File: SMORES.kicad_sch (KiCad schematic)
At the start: 41 parts, among them J1 USB_C_Receptacle_USB2.0_14P, SW1 Power, SW2 Reset, SW3 SW0, U2 BQ24075RGT, U3 ICM45686, U4 XC6220B331MR, U5 1532H, U6 QMC6309, U7 E73-2G4M08S1C, Y2 32.768kHz

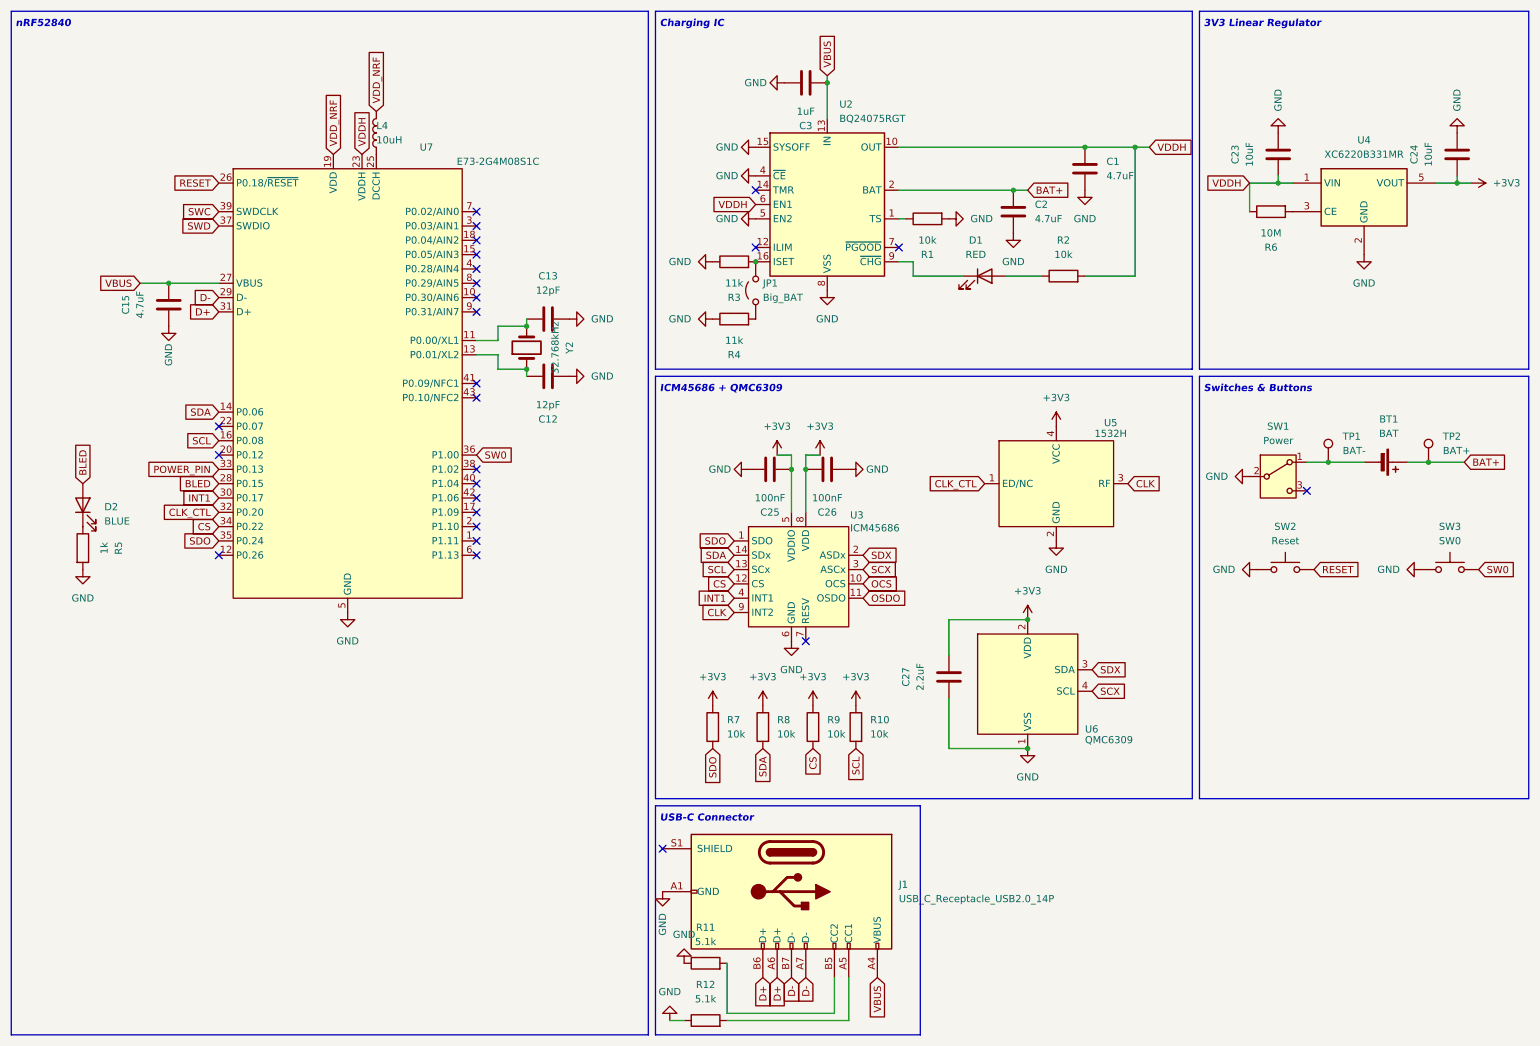
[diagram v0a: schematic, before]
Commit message: Remove LDO and peripherals
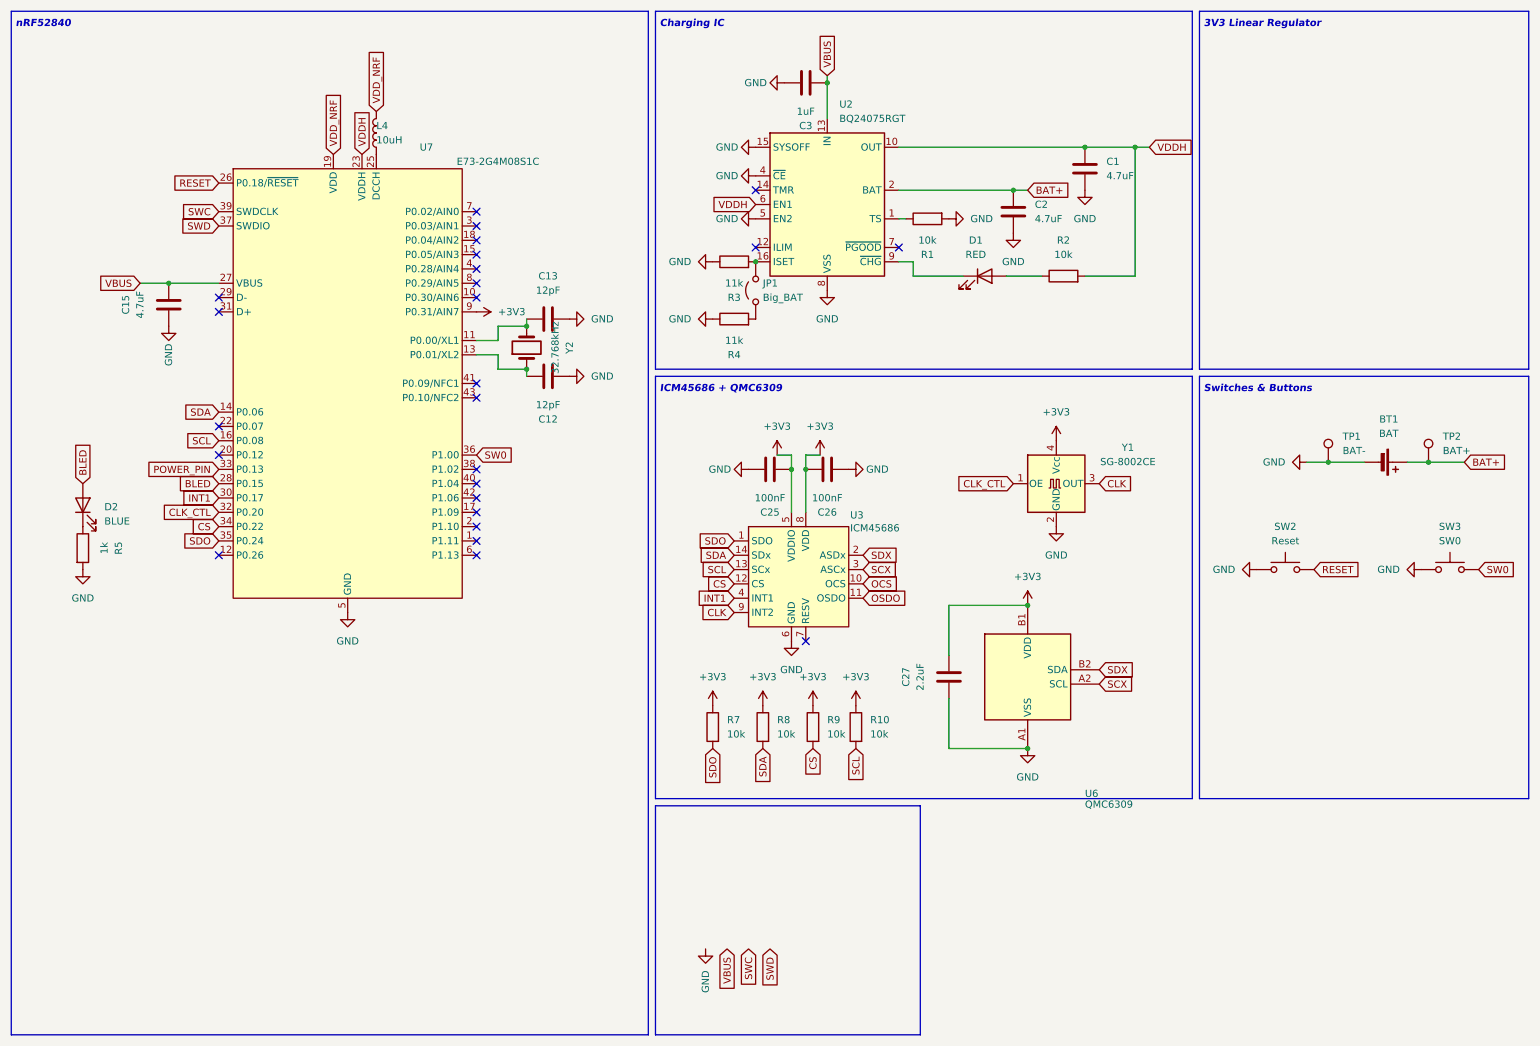
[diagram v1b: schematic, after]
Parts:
- removed C23, C24: 10uF, Capacitor_SMD:C_0603_1608Metric, symbol Device:C
- removed J1: USB_C_Receptacle_USB2.0_14P, Connector_USB:USB_C_Receptacle_HRO_TYPE-C-31-M-12, symbol Connector:USB_C_Receptacle_USB2.0_14P
- removed R11, R12: 5.1k, Capacitor_SMD:C_0603_1608Metric, symbol Device:R
- removed R6: 10M, Resistor_SMD:R_0402_1005Metric, symbol Device:R
- removed SW1: Power, SMORES:SW_SPDT_Shouhan_MSK12C02, symbol Switch:SW_SPDT
- removed U4: XC6220B331MR, Package_TO_SOT_SMD:SOT-23-5, symbol Regulator_Linear:XC6220B331MR
- removed U5: 1532H, Crystal:Crystal_SMD_3225-4Pin_3.2x2.5mm, symbol SlimeVR_Smol:1532H
- added Y1: SG-8002CE, Oscillator:Oscillator_SMD_SeikoEpson_SG8002CE-4Pin_3.2x2.5mm, symbol Oscillator:SG-8002CE
- U3: footprint ICM_SLIME:IC_ICM-45686 -> ICM-45686:IC_ICM-45686
- U6: footprint Custom:WLCSP-4_0.8x0.8mm_Layout2x2_P0.4mm -> QMC6309:IC_QMC6309; symbol SlimeVR_Smol:QMC6309 -> QMC6309:QMC6309
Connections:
- net +3V3: now also U6.B1 (VDD), U7.9 (P0.31/AIN7), Y1.4 (Vcc); no longer U6.2 (VDD)
- net CLK: now also Y1.3 (OUT)
- net CLK_CTL: now also Y1.1 (OE)
- net GND: now also BT1.2 (-), TP1.1, U6.A1 (VSS), Y1.2 (GND); no longer U6.1 (VSS)
- net SCX: now also U6.A2 (SCL); no longer U6.4 (SCL)
- net SDX: now also U6.B2 (SDA); no longer U6.3 (SDA)
- net D+: no longer names the net of U7.31 (D+)
- net D-: no longer names the net of U7.29 (D-)
- no-connect marks 26 -> 25
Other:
- note removed: "USB-C Connector"
- moved on the sheet: U6

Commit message: Redesign entire PCB and make it smaller
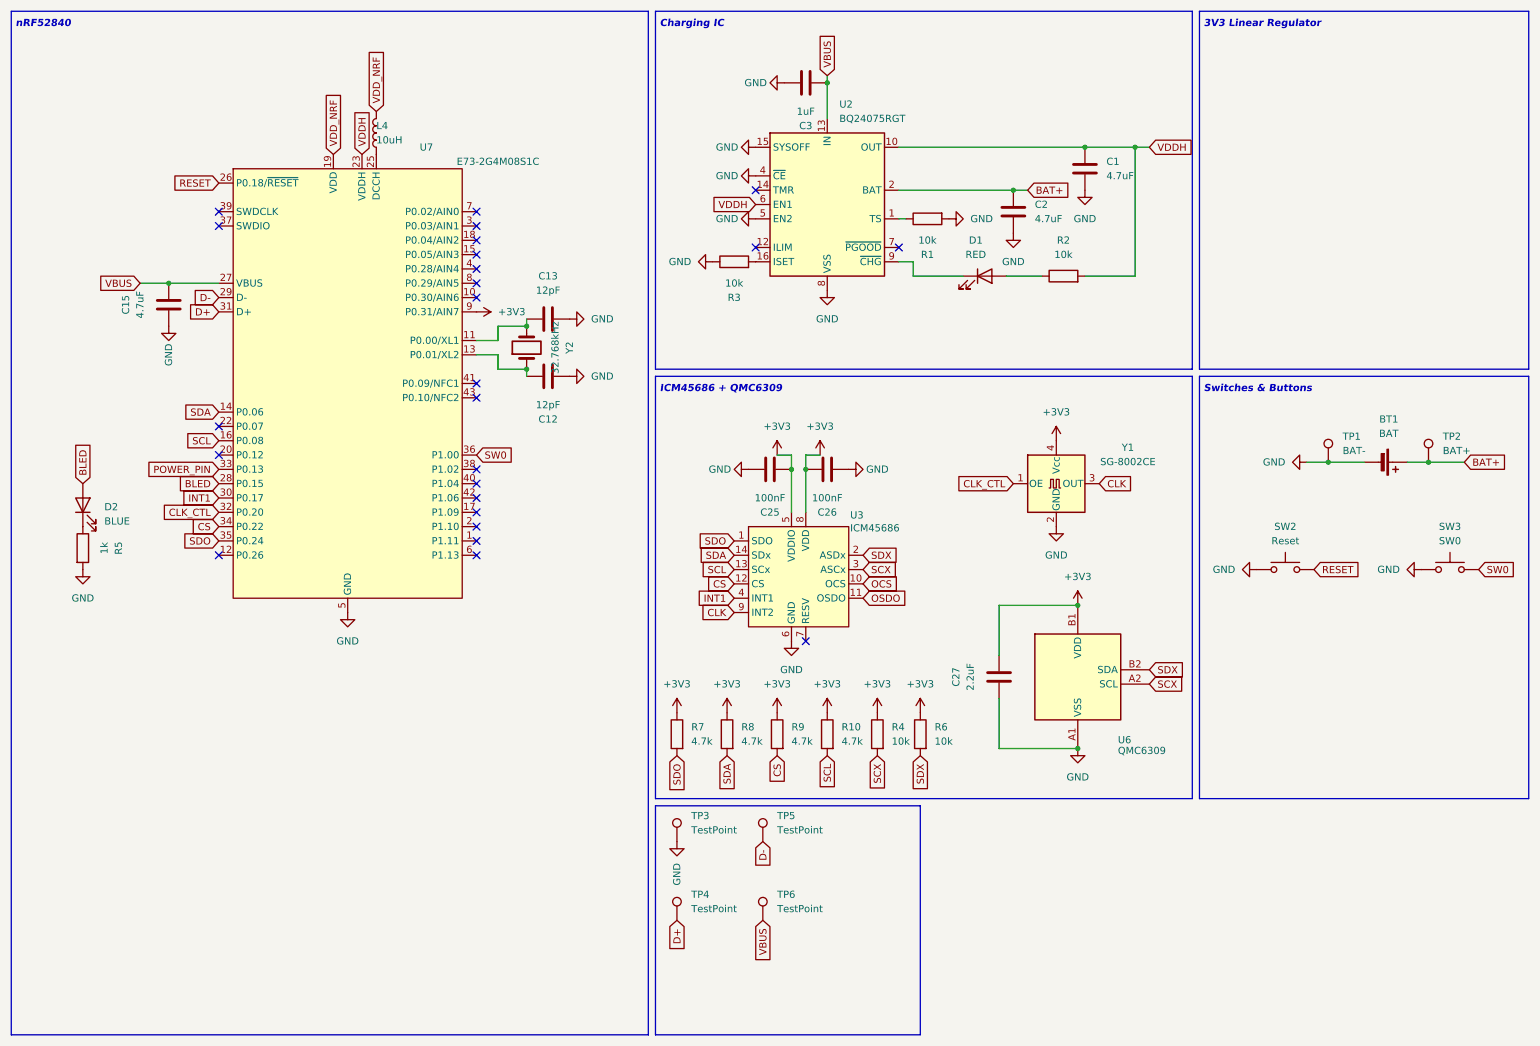
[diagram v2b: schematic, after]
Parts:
- removed JP1: Big_BAT, Jumper:SolderJumper-2_P1.3mm_Open_Pad1.0x1.5mm, symbol Jumper:Jumper_2_Open
- added R6: 10k, Resistor_SMD:R_0402_1005Metric, symbol Device:R
- added TP3, TP4, TP5, TP6: TestPoint, TestPoint:TestPoint_Pad_D1.5mm, symbol Connector:TestPoint
- C1, C15, C2, C27, C3: footprint Capacitor_SMD:C_0603_1608Metric -> Capacitor_SMD:C_0402_1005Metric
- C12, C13: footprint Capacitor_SMD:C_0402_1005Metric -> Capacitor_SMD:C_0603_1608Metric_Pad1.08x0.95mm_HandSolder
- L4: footprint Inductor_SMD:L_0603_1608Metric -> Inductor_SMD:L_0603_1608Metric_Pad1.05x0.95mm_HandSolder
- R10, R7, R8, R9: value 10k -> 4.7k
- R3, R4: value 11k -> 10k
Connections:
- net +3V3: now also R4.1, R6.1
- net GND: now also TP3.1; no longer R4.1
- net SCX: now also R4.2
- net SDX: now also R6.2
- net VBUS: now also TP6.1
- net D-: now reaches U7.29 (D-)
- net D-: now also TP5.1
- net D+: now reaches U7.31 (D+)
- net D+: now also TP4.1
- net SWC: no longer names the net of U7.39 (SWDCLK)
- net SWD: no longer names the net of U7.37 (SWDIO)
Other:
- moved on the sheet: C27, R10, R7, R8, R9, U6
